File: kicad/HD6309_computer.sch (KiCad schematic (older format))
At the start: 56 parts, among them M1 MountingHole3mm, M2 MountingHole3mm, M3 MountingHole3mm, M4 MountingHole3mm, P1 USB_B, P2 CONN_01X02, P3 CONN_01X08, P4 CONN_01X10, P5 CONN_01X05, Q1 2N3904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

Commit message: Updated schematic with DRC fixes and TODOs
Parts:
- C1, C2: symbol CP_Small -> HD6309_computer-rescue:CP_Small
- C10, C11, C12, C3, C4, C5, C6, C7, C8, C9, C? (x4): symbol C_Small -> HD6309_computer-rescue:C_Small
- D1, D2, D3: symbol LED -> HD6309_computer-rescue:LED
- LOGO1, LOGO2, LOGO3: symbol Logo -> HD6309_computer-rescue:Logo
- M1, M2, M3, M4: symbol MountingHole3mm -> HD6309_computer-rescue:MountingHole3mm
- P1: symbol USB_B -> HD6309_computer-rescue:USB_B
- P2: symbol CONN_01X02 -> HD6309_computer-rescue:CONN_01X02
- P3: symbol CONN_01X08 -> HD6309_computer-rescue:CONN_01X08
- P4: symbol CONN_01X10 -> HD6309_computer-rescue:CONN_01X10
- P5: symbol CONN_01X05 -> HD6309_computer-rescue:CONN_01X05
- Q1: symbol Q_NPN_EBC -> HD6309_computer-rescue:Q_NPN_EBC
- R1, R10, R11, R2, R3, R4, R5, R6, R7, R8, R9: symbol R_Small -> HD6309_computer-rescue:R_Small
- SW1: symbol SW_PUSH_SMALL_H -> HD6309_computer-rescue:SW_PUSH_SMALL_H
- U1: symbol HD63C09 -> HD6309_computer-rescue:HD63C09
- U10: symbol AS6C8008 -> HD6309_computer-rescue:AS6C8008
- U11: symbol SC16C550B -> HD6309_computer-rescue:SC16C550B
- U12: symbol AT28C64B -> HD6309_computer-rescue:AT28C64B
- U2, U4: symbol ATF16V8B -> HD6309_computer-rescue:ATF16V8B
- U3, U9: symbol Oscillator7x5 -> HD6309_computer-rescue:Oscillator7x5
- U5, U8: symbol 74HC541 -> HD6309_computer-rescue:74HC541
- U6: symbol 74HCT245 -> HD6309_computer-rescue:74HCT245
- U7: symbol 74HC574 -> HD6309_computer-rescue:74HC574
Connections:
- no-connect marks 41 -> 44
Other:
- note added: "Add MCP2200 USB UART."
- note added: "FIXME: change to pull-up/down resistors."

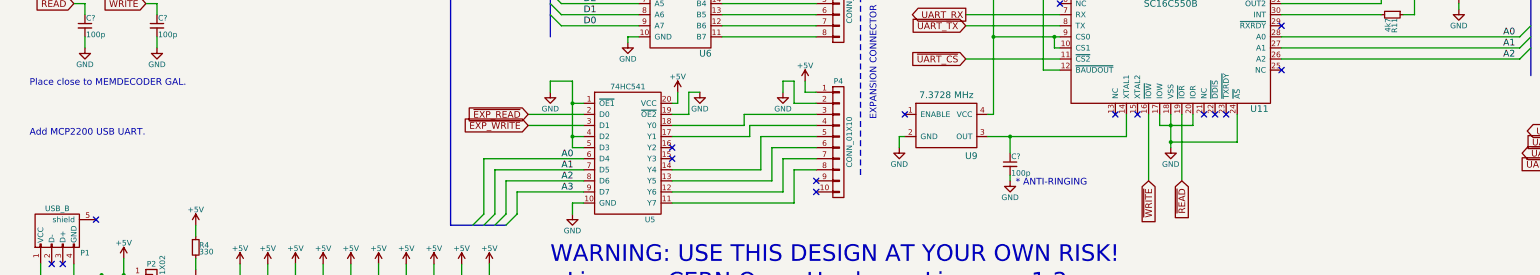
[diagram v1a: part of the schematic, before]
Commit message: Fixed IO decoder GAL?
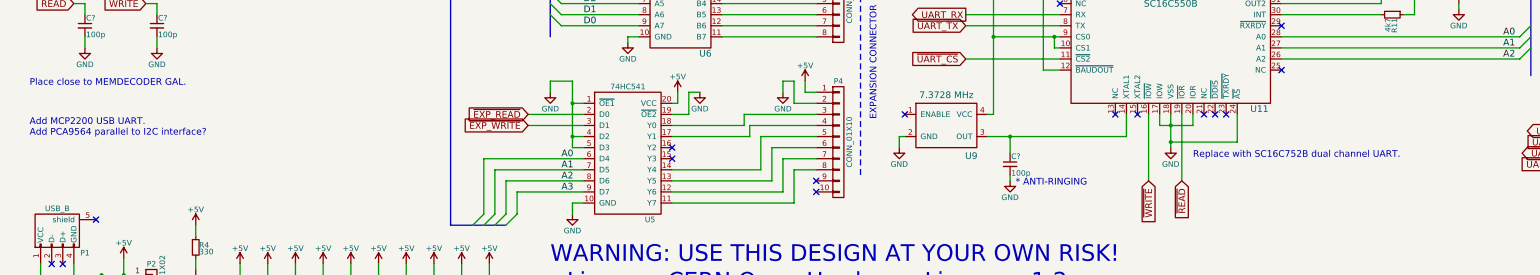
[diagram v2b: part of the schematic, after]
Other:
- note added: "Add MCP2200 USB UART.\nAdd PCA9564 parallel to I2C interface?"
- note added: "Replace with SC16C752B dual channel UART."
- note removed: "Add MCP2200 USB UART."
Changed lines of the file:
@@
 NoConn ~ 7800 9600
 NoConn ~ 7800 9700
+Text Notes 6750 6800 0    60   ~ 0
+FIXME: change to pull-up/down resistors.
+Text Notes 700  9200 0    60   ~ 0
+Add MCP2200 USB UART.\nAdd PCA9564 parallel to I2C interface?
 Wire Bus Line
 	1050 6650 1500 6650
@@
 Wire Bus Line
 	11250 600  11250 4800
-Text Notes 6750 6800 0    60   ~ 0
-FIXME: change to pull-up/down resistors.
-Text Notes 700  9200 0    60   ~ 0
-Add MCP2200 USB UART.
+Text Notes 11200 9400 0    60   ~ 0
+Replace with SC16C752B dual channel UART.
 $EndSCHEMATC

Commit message: Added Kicad rescue libraries
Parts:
- C1, C2: symbol HD6309_computer-rescue:CP_Small -> HD6309_computer-rescue:CP_Small-HD6309_computer-rescue
- C10, C11, C12, C3, C4, C5, C6, C7, C8, C9, C? (x4): symbol HD6309_computer-rescue:C_Small -> HD6309_computer-rescue:C_Small-HD6309_computer-rescue
- Q1: symbol HD6309_computer-rescue:Q_NPN_EBC -> HD6309_computer-rescue:Q_NPN_EBC-HD6309_computer-rescue
- R1, R10, R11, R2, R3, R4, R5, R6, R7, R8, R9: symbol HD6309_computer-rescue:R_Small -> HD6309_computer-rescue:R_Small-HD6309_computer-rescue
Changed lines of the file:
@@
 EESchema Schematic File Version 4
 LIBS:HD6309_computer-cache
-EELAYER 30 0
+EELAYER 29 0
 EELAYER END
 $Descr A3 16535 11693
@@
 NoConn ~ 2950 2350
 $Comp
-L HD6309_computer-rescue:R_Small R5
+L HD6309_computer-rescue:R_Small-HD6309_computer-rescue R5
 U 1 1 58E38FDA
 P 3000 1100
@@
 $EndComp
 $Comp
-L HD6309_computer-rescue:R_Small R1
+L HD6309_computer-rescue:R_Small-HD6309_computer-rescue R1
 U 1 1 58E3BB2F
 P 1350 1100
@@
 ~RAM_FIX
 $Comp
-L HD6309_computer-rescue:R_Small R6
+L HD6309_computer-rescue:R_Small-HD6309_computer-rescue R6
 U 1 1 58E17CB6
 P 3250 1100
@@
 $EndComp
 $Comp
-L HD6309_computer-rescue:R_Small R7
+L HD6309_computer-rescue:R_Small-HD6309_computer-rescue R7
 U 1 1 58E17CE9
 P 3500 1100
@@
 WRITE_MAP
 $Comp
-L HD6309_computer-rescue:R_Small R8
+L HD6309_computer-rescue:R_Small-HD6309_computer-rescue R8
 U 1 1 58E272B3
 P 3750 1100
@@
 NoConn ~ 1850 2250
 $Comp
-L HD6309_computer-rescue:R_Small R2
+L HD6309_computer-rescue:R_Small-HD6309_computer-rescue R2
 U 1 1 58E2F507
 P 1550 1100
@@
 $EndComp
 $Comp
-L HD6309_computer-rescue:R_Small R9
+L HD6309_computer-rescue:R_Small-HD6309_computer-rescue R9
 U 1 1 58E8B4C5
 P 12600 6900
@@
 $EndComp
 $Comp
-L HD6309_computer-rescue:R_Small R10
+L HD6309_computer-rescue:R_Small-HD6309_computer-rescue R10
 U 1 1 58E8B552
 P 12900 6900
@@
 NoConn ~ 8600 9000
 $Comp
-L HD6309_computer-rescue:CP_Small C1
+L HD6309_computer-rescue:CP_Small-HD6309_computer-rescue C1
 U 1 1 58E9C69F
 P 1350 10650
@@
 ~INT
 $Comp
-L HD6309_computer-rescue:Q_NPN_EBC Q1
+L HD6309_computer-rescue:Q_NPN_EBC-HD6309_computer-rescue Q1
 U 1 1 58EA095E
 P 13500 7800
@@
 $EndComp
 $Comp
-L HD6309_computer-rescue:R_Small R11
+L HD6309_computer-rescue:R_Small-HD6309_computer-rescue R11
 U 1 1 58EA1A1D
 P 13000 8100
@@
 $EndComp
 $Comp
-L HD6309_computer-rescue:CP_Small C2
+L HD6309_computer-rescue:CP_Small-HD6309_computer-rescue C2
 U 1 1 58EA56A3
 P 5700 2350
@@
 ~EXPANSION_OE
 $Comp
-L HD6309_computer-rescue:R_Small R3
+L HD6309_computer-rescue:R_Small-HD6309_computer-rescue R3
 U 1 1 58E8524E
 P 1750 1100
@@
 $EndComp
 $Comp
-L HD6309_computer-rescue:R_Small R4
+L HD6309_computer-rescue:R_Small-HD6309_computer-rescue R4
 U 1 1 58E9A823
 P 2200 10200
@@
 Connection ~ 1550 10450
 $Comp
-L HD6309_computer-rescue:C_Small C3
+L HD6309_computer-rescue:C_Small-HD6309_computer-rescue C3
 U 1 1 58E9DBDA
 P 2600 10600
@@
 $EndComp
 $Comp
-L HD6309_computer-rescue:C_Small C4
+L HD6309_computer-rescue:C_Small-HD6309_computer-rescue C4
 U 1 1 58E9DD41
 P 2850 10600
@@
 $EndComp
 $Comp
-L HD6309_computer-rescue:C_Small C5
+L HD6309_computer-rescue:C_Small-HD6309_computer-rescue C5
 U 1 1 58E9DDC6
 P 3100 10600
@@
 $EndComp
 $Comp
-L HD6309_computer-rescue:C_Small C6
+L HD6309_computer-rescue:C_Small-HD6309_computer-rescue C6
 U 1 1 58E9DE52
 P 3350 10600
@@
 $EndComp
 $Comp
-L HD6309_computer-rescue:C_Small C7
+L HD6309_computer-rescue:C_Small-HD6309_computer-rescue C7
 U 1 1 58E9DF79
 P 3600 10600
@@
 $EndComp
 $Comp
-L HD6309_computer-rescue:C_Small C8
+L HD6309_computer-rescue:C_Small-HD6309_computer-rescue C8
 U 1 1 58E9DF7F
 P 3850 10600
@@
 $EndComp
 $Comp
-L HD6309_computer-rescue:C_Small C9
+L HD6309_computer-rescue:C_Small-HD6309_computer-rescue C9
 U 1 1 58E9DF85
 P 4100 10600
@@
 $EndComp
 $Comp
-L HD6309_computer-rescue:C_Small C10
+L HD6309_computer-rescue:C_Small-HD6309_computer-rescue C10
 U 1 1 58E9DF8B
 P 4350 10600
@@
 $EndComp
 $Comp
-L HD6309_computer-rescue:C_Small C11
+L HD6309_computer-rescue:C_Small-HD6309_computer-rescue C11
 U 1 1 58E9E019
 P 4600 10600
@@
 $EndComp
 $Comp
-L HD6309_computer-rescue:C_Small C12
+L HD6309_computer-rescue:C_Small-HD6309_computer-rescue C12
 U 1 1 58E9E01F
 P 4850 10600
@@
 	2500 6200 2700 6200
 $Comp
-L HD6309_computer-rescue:C_Small C?
+L HD6309_computer-rescue:C_Small-HD6309_computer-rescue C?
 U 1 1 59101EB6
 P 5200 1800
@@
 * ANTI-RINGING
 $Comp
-L HD6309_computer-rescue:C_Small C?
+L HD6309_computer-rescue:C_Small-HD6309_computer-rescue C?
 U 1 1 59103C0C
 P 9550 9450
@@
 ~READ
 $Comp
-L HD6309_computer-rescue:C_Small C?
+L HD6309_computer-rescue:C_Small-HD6309_computer-rescue C?
 U 1 1 5910A517
 P 1200 8200
@@
 ~WRITE
 $Comp
-L HD6309_computer-rescue:C_Small C?
+L HD6309_computer-rescue:C_Small-HD6309_computer-rescue C?
 U 1 1 5910B611
 P 1850 8200
@@
 Text Notes 700  9200 0    60   ~ 0
 Add MCP2200 USB UART.\nAdd PCA9564 parallel to I2C interface?
+Text Notes 11200 9400 0    60   ~ 0
+Replace with SC16C752B dual channel UART.
 Wire Bus Line
 	1050 6650 1500 6650
@@
 Wire Bus Line
 	11250 600  11250 4800
-Text Notes 11200 9400 0    60   ~ 0
-Replace with SC16C752B dual channel UART.
 $EndSCHEMATC
